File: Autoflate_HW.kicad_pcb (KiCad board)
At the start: 2 copper layers, 115 x 78 mm, 69 parts, among them J1 JST_XH_3, J10 JST_VH_2, J11 JST_VH_2, J12 JST_XH_3, J13 Header_1, J2 JST_VH_3, J3 Conn_01x04_Male, J6 JST_XH_4, J7 Header_2, J8 Header_4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

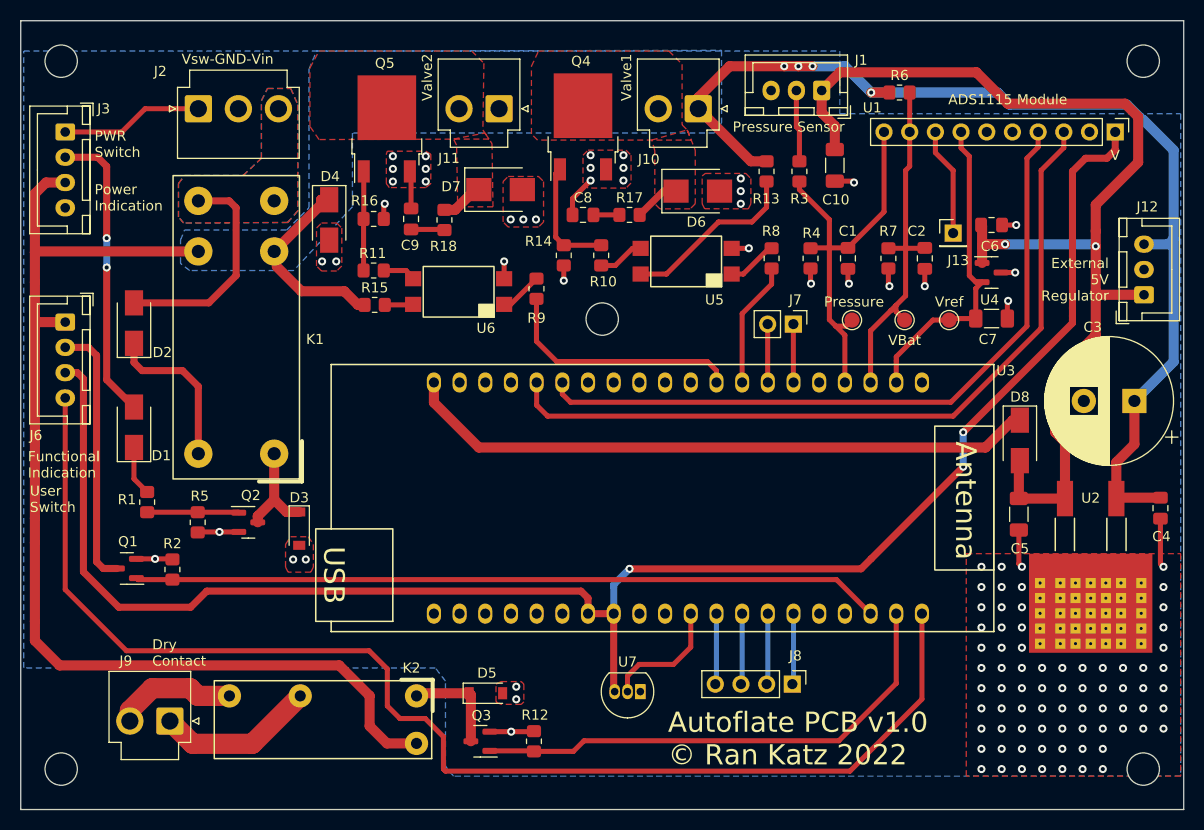
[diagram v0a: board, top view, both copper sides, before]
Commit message: added buzzer connection
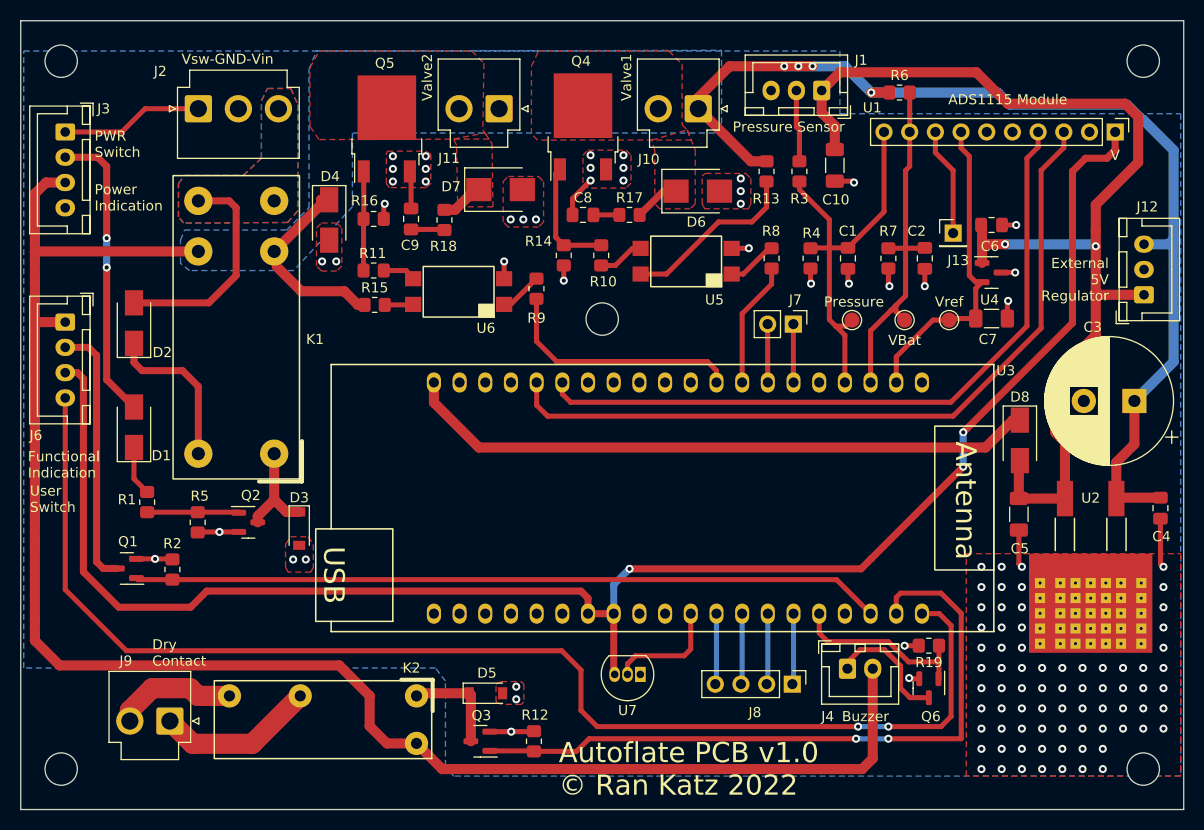
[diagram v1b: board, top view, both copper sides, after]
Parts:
- added J4: JST_XH_2, Connector_JST:JST_XH_B2B-XH-A_1x02_P2.50mm_Vertical, F.Cu at (111.8, 91.1)
- added Q6: AO3400A, Package_TO_SOT_SMD:SOT-23, F.Cu at (119.8, 93.0)
- added R19: 10k, Resistor_SMD:R_0805_2012Metric_Pad1.20x1.40mm_HandSolder, F.Cu at (119.8, 88.8)
- moved U7 1.70 mm to (91.3, 91.6)
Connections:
- U3 pad 36: unconnected-(U3-Pad36) -> /Buzzer
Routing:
- net +12V: track 239.4 -> 294.9 mm
- net Net-(Q3-Pad1): track 49.9 -> 68.6 mm, vias 0 -> 2
- net /Buzzer: track 0.00 -> 18.2 mm
- net Net-(J4-Pad1): track 0.00 -> 12.4 mm
- net GND: track 48.1 -> 50.5 mm, vias 113 -> 115
- net /VDD3V3: track 168.1 -> 166.4 mm
- net /Temp_DQ: track 12.3 -> 11.4 mm
- net /User_SW: track 126.5 -> 127.3 mm, vias 0 -> 2
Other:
- board text added: "Buzzer"

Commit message: Updated revision, added revision description
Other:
- board text added: "Autoflate PCB v1.1 © Ran Katz 2022"
- board text added: "Revision Control: V1.0: Baseline V1.1: Added Buzzer connection"
- board text removed: "Autoflate PCB v1.0 © Ran Katz 2022"
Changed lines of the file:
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@@
   (title_block
     (title "Autoflate - Tire inflator controller board")
+    (date "2022-11-03")
+    (rev "1.1")
     (company "NIghtmechanics")
     (comment 4 "AISLER Project ID: KECQLVEM")
@@
   (gr_rect (start 30 30) (end 145 102) (layer "Dwgs.User") (width 0.15) (fill none))
   (gr_rect (start 30 27) (end 145 105) (layer "Edge.Cuts") (width 0.1) (fill none))
+  (gr_text "Revision Control:\nV1.0: Baseline\nV1.1: Added Buzzer connection" (at 120 69.4) (layer "B.SilkS")
+    (effects (font (size 1.5 1.5) (thickness 0.3)) (justify left mirror))
+  )
   (gr_text "Valve1" (at 89.9 32.6 90) (layer "F.SilkS")
     (effects (font (size 1 1) (thickness 0.15)))
@@
     (effects (font (size 1 1) (thickness 0.15)) (justify left))
   )
-  (gr_text "Autoflate PCB v1.0\n© Ran Katz 2022" (at 83.2 101) (layer "F.SilkS")
+  (gr_text "Autoflate PCB v1.1\n© Ran Katz 2022" (at 83.2 101) (layer "F.SilkS")
     (effects (font (size 2 2) (thickness 0.15)) (justify left))
   )
